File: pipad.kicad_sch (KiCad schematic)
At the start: 2 parts, among them J3 Conn_02x20_Odd_Even, J5 Conn_01x03

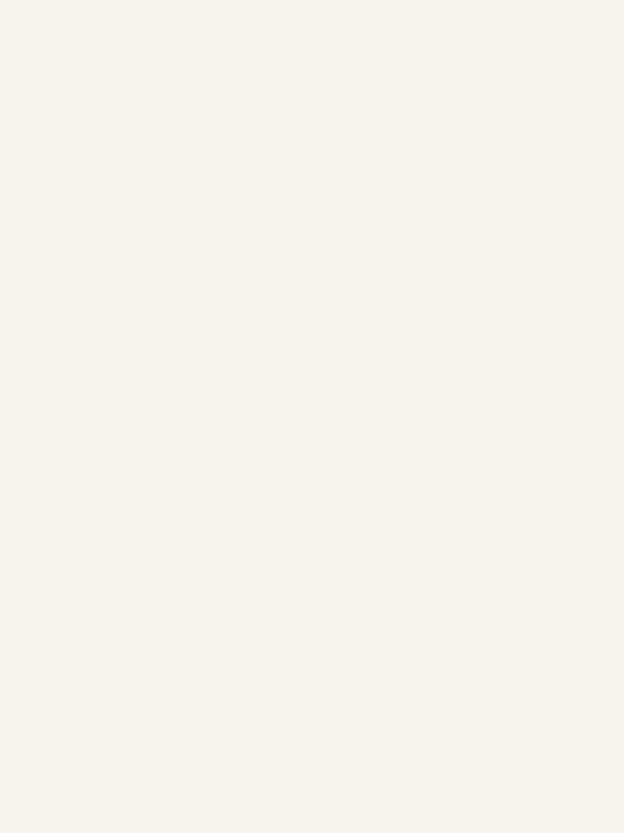
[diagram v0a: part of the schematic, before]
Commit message: refactor gt9113_breakout into hierarchical sheet.
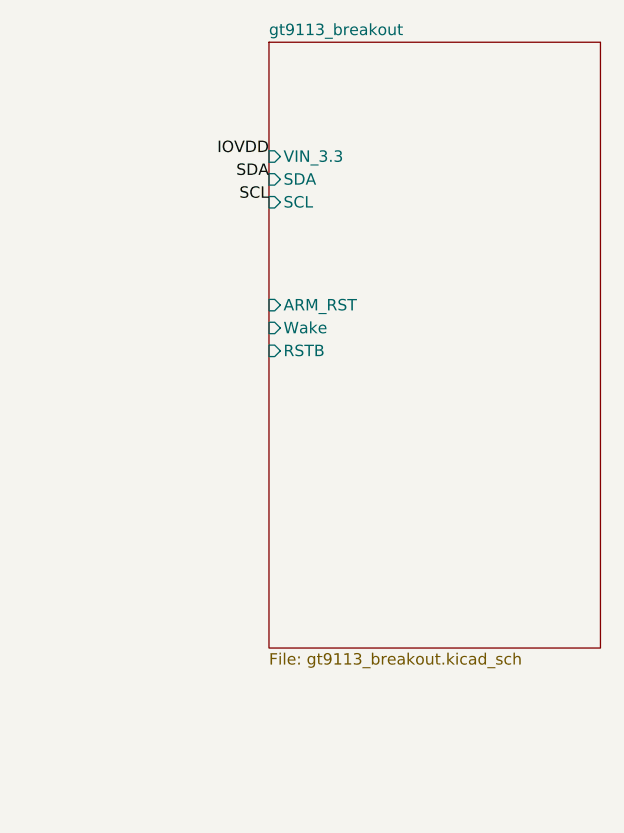
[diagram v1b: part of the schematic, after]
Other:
- added sheet gt9113_breakout (gt9113_breakout.kicad_sch)
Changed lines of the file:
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@@
     (effects (font (size 1.27 1.27)) (justify left bottom))
+  )
+  (label "IOVDD" (at 167.64 50.8 180)
+    (effects (font (size 1.27 1.27)) (justify right bottom))
+  )
+  (label "SDA" (at 167.64 53.34 180)
+    (effects (font (size 1.27 1.27)) (justify right bottom))
+  )
+  (label "SCL" (at 167.64 55.88 180)
+    (effects (font (size 1.27 1.27)) (justify right bottom))
   )
   (symbol (lib_id "power:PWR_FLAG") (at 34.29 156.21 0) (unit 1)
@@
     )
   )
+  (sheet (at 167.64 38.1) (size 36.83 67.31) (fields_autoplaced)
+    (stroke (width 0.0006) (type solid) (color 0 0 0 0))
+    (fill (color 0 0 0 0.0000))
+    (property "Sheet name" "gt9113_breakout" (id 0) (at 167.64 37.4643 0)
+      (effects (font (size 1.27 1.27)) (justify left bottom))
+    )
+    (property "Sheet file" "gt9113_breakout.kicad_sch" (id 1) (at 167.64 105.9187 0)
+      (effects (font (size 1.27 1.27)) (justify left top))
+    )
+    (pin "VIN_3.3" input (at 167.64 50.8 180)
+      (effects (font (size 1.27 1.27)) (justify left))
+    )
+    (pin "SDA" input (at 167.64 53.34 180)
+      (effects (font (size 1.27 1.27)) (justify left))
+    )
+    (pin "SCL" input (at 167.64 55.88 180)
+      (effects (font (size 1.27 1.27)) (justify left))
+    )
+    (pin "ARM_RST" input (at 167.64 67.31 180)
+      (effects (font (size 1.27 1.27)) (justify left))
+    )
+    (pin "Wake" input (at 167.64 69.85 180)
+      (effects (font (size 1.27 1.27)) (justify left))
+    )
+    (pin "RSTB" input (at 167.64 72.39 180)
+      (effects (font (size 1.27 1.27)) (justify left))
+    )
+  )
   (sheet_instances
     (path "/" (page "1"))
     (path "/00000000-0000-0000-0000-00006026a3be/" (page "2"))
     (path "/00000000-0000-0000-0000-00006026a3be/00000000-0000-0000-0000-000060276bea/" (page "4"))
+    (path "/4ecc04d7-c0c4-4778-83ba-d295a895ebe9/" (page "5"))
     (path "/00000000-0000-0000-0000-00006026a3be/e9fc4bb6-5bde-4905-9630-250663643427/" (page " "))
   )
@@
       (reference "U3") (unit 1) (value "TPA2006D1DRBR") (footprint "footprints:TPA2006D1DRBR")
     )
+    (path "/4ecc04d7-c0c4-4778-83ba-d295a895ebe9/00000000-0000-0000-0000-0000600d74cd"
+      (reference "#FLG0102") (unit 1) (value "PWR_FLAG") (footprint "")
+    )
+    (path "/4ecc04d7-c0c4-4778-83ba-d295a895ebe9/00000000-0000-0000-0000-000060028f86"
+      (reference "#PWR010") (unit 1) (value "GND") (footprint "")
+    )
+    (path "/4ecc04d7-c0c4-4778-83ba-d295a895ebe9/00000000-0000-0000-0000-000060029001"
+      (reference "#PWR023") (unit 1) (value "GND") (footprint "")
+    )
+    (path "/4ecc04d7-c0c4-4778-83ba-d295a895ebe9/00000000-0000-0000-0000-000060029007"
+      (reference "#PWR033") (unit 1) (value "GND") (footprint "")
+    )
+    (path "/4ecc04d7-c0c4-4778-83ba-d295a895ebe9/00000000-0000-0000-0000-0000603613b4"
+      (reference "#PWR0101") (unit 1) (value "GND") (footprint "")
+    )
+    (path "/4ecc04d7-c0c4-4778-83ba-d295a895ebe9/00000000-0000-0000-0000-0000603614b1"
+      (reference "#PWR0102") (unit 1) (value "GND") (footprint "")
+    )
+    (path "/4ecc04d7-c0c4-4778-83ba-d295a895ebe9/00000000-0000-0000-0000-0000604218d4"
+      (reference "#PWR0103") (unit 1) (value "GND") (footprint "")
+    )
+    (path "/4ecc04d7-c0c4-4778-83ba-d295a895ebe9/00000000-0000-0000-0000-00006042145b"
+      (reference "#PWR0104") (unit 1) (value "GND") (footprint "")
+    )
+    (path "/4ecc04d7-c0c4-4778-83ba-d295a895ebe9/00000000-0000-0000-0000-0000604214a2"
+      (reference "#PWR0105") (unit 1) (value "GND") (footprint "")
+    )
+    (path "/4ecc04d7-c0c4-4778-83ba-d295a895ebe9/00000000-0000-0000-0000-00006042f1b0"
+      (reference "#PWR0106") (unit 1) (value "GND") (footprint "")
+    )
+    (path "/4ecc04d7-c0c4-4778-83ba-d295a895ebe9/00000000-0000-0000-0000-0000604338e7"
+      (reference "#PWR0107") (unit 1) (value "GND") (footprint "")
+    )
+    (path "/4ecc04d7-c0c4-4778-83ba-d295a895ebe9/00000000-0000-0000-0000-000060439719"
+      (reference "#PWR0108") (unit 1) (value "GND") (footprint "")
+    )
+    (path "/4ecc04d7-c0c4-4778-83ba-d295a895ebe9/00000000-0000-0000-0000-00006041d916"
+      (reference "C1") (unit 1) (value "2.2uF") (footprint "Capacitor_SMD:C_0402_1005Metric")
+    )
+    (path "/4ecc04d7-c0c4-4778-83ba-d295a895ebe9/00000000-0000-0000-0000-00006041dee8"
+      (reference "C2") (unit 1) (value "2.2uF") (footprint "Capacitor_SMD:C_0402_1005Metric")
+    )
+    (path "/4ecc04d7-c0c4-4778-83ba-d295a895ebe9/00000000-0000-0000-0000-00006041e2b4"
+      (reference "C3") (unit 1) (value "2.2uF") (footprint "Capacitor_SMD:C_0402_1005Metric")
+    )
+    (path "/4ecc04d7-c0c4-4778-83ba-d295a895ebe9/00000000-0000-0000-0000-000060049eec"
+      (reference "J1") (unit 1) (value "Conn_01x09_Male") (footprint "Connector_PinHeader_2.54mm:PinHeader_1x09_P2.54mm_Vertical")
+    )
+    (path "/4ecc04d7-c0c4-4778-83ba-d295a895ebe9/00000000-0000-0000-0000-000060028f6e"
+      (reference "J7") (unit 1) (value "504740-5100") (footprint "footprints:504740-5100")
+    )
+    (path "/4ecc04d7-c0c4-4778-83ba-d295a895ebe9/00000000-0000-0000-0000-000060028f74"
+      (reference "J7") (unit 1) (value "504740-5100") (footprint "footprints:504740-5100")
+    )
+    (path "/4ecc04d7-c0c4-4778-83ba-d295a895ebe9/00000000-0000-0000-0000-000060028f7a"
+      (reference "J8") (unit 1) (value "504740-5100") (footprint "footprints:504740-5100")
+    )
+    (path "/4ecc04d7-c0c4-4778-83ba-d295a895ebe9/00000000-0000-0000-0000-000060028f80"
+      (reference "J8") (unit 1) (value "504740-5100") (footprint "footprints:504740-5100")
+    )
+    (path "/4ecc04d7-c0c4-4778-83ba-d295a895ebe9/00000000-0000-0000-0000-000060432c0a"
+      (reference "R1") (unit 1) (value "0R/DNF") (footprint "Resistor_SMD:R_0402_1005Metric")
+    )
+    (path "/4ecc04d7-c0c4-4778-83ba-d295a895ebe9/00000000-0000-0000-0000-0000604322a7"
+      (reference "R2") (unit 1) (value "0R/DNF") (footprint "Resistor_SMD:R_0402_1005Metric")
+    )
+    (path "/4ecc04d7-c0c4-4778-83ba-d295a895ebe9/00000000-0000-0000-0000-000060427deb"
+      (reference "R3") (unit 1) (value "300k/DNF") (footprint "Resistor_SMD:R_0402_1005Metric")
+    )
+    (path "/4ecc04d7-c0c4-4778-83ba-d295a895ebe9/00000000-0000-0000-0000-000060371774"
+      (reference "U1") (unit 1) (value "GT9113") (footprint "footprints:GT9113")
+    )
     (path "/00000000-0000-0000-0000-00006026a3be/e9fc4bb6-5bde-4905-9630-250663643427/fd649b90-fe8e-4ecf-a531-c62c874ce18c"

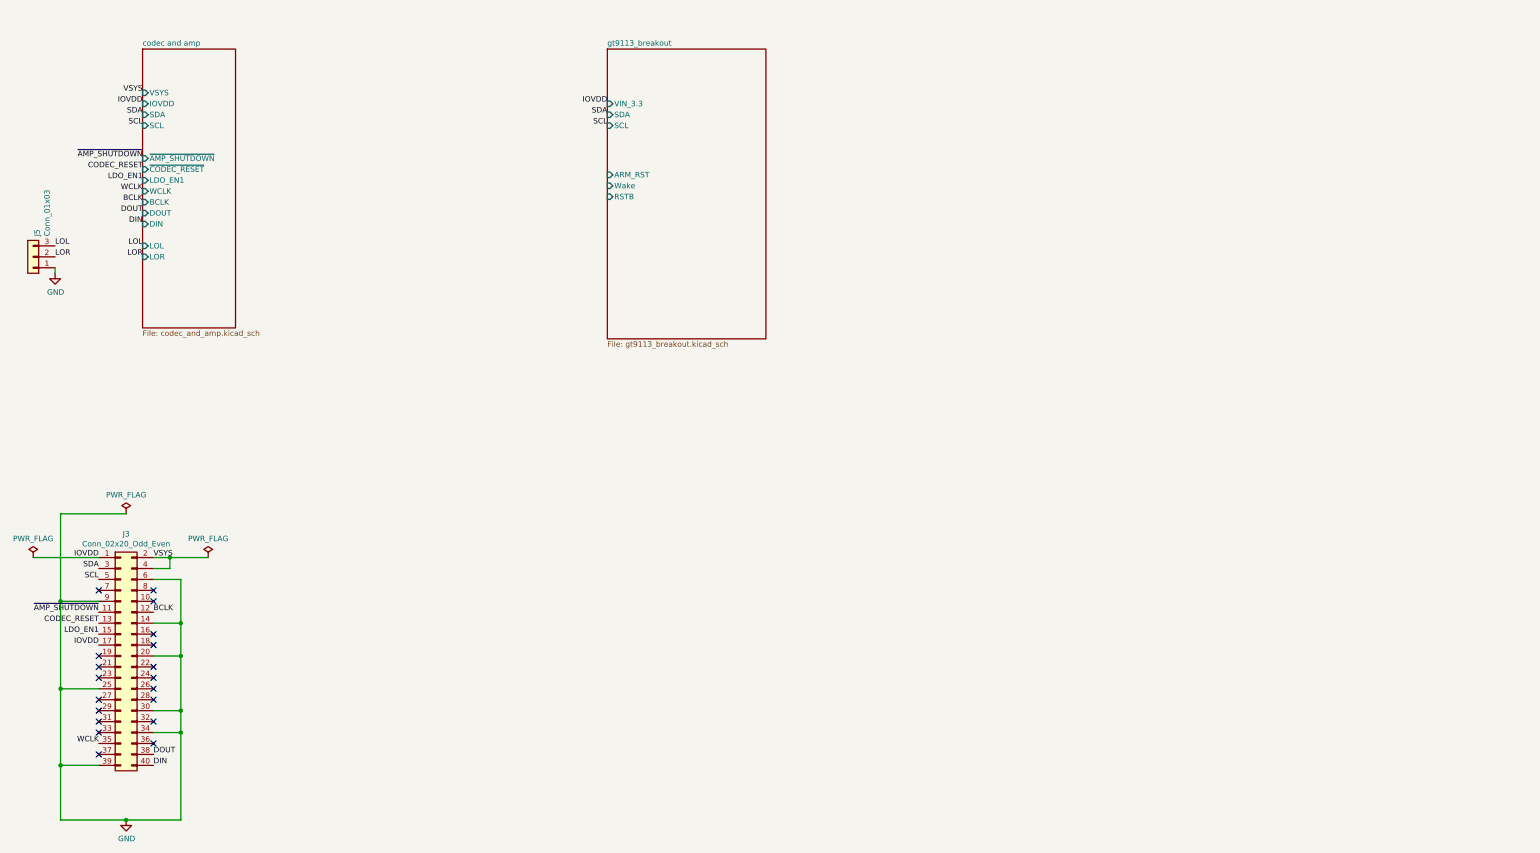
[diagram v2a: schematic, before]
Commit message: Import LVDS schematic as hierarchical sheet. Add level shifters for I2C and EN/IRQ pins.
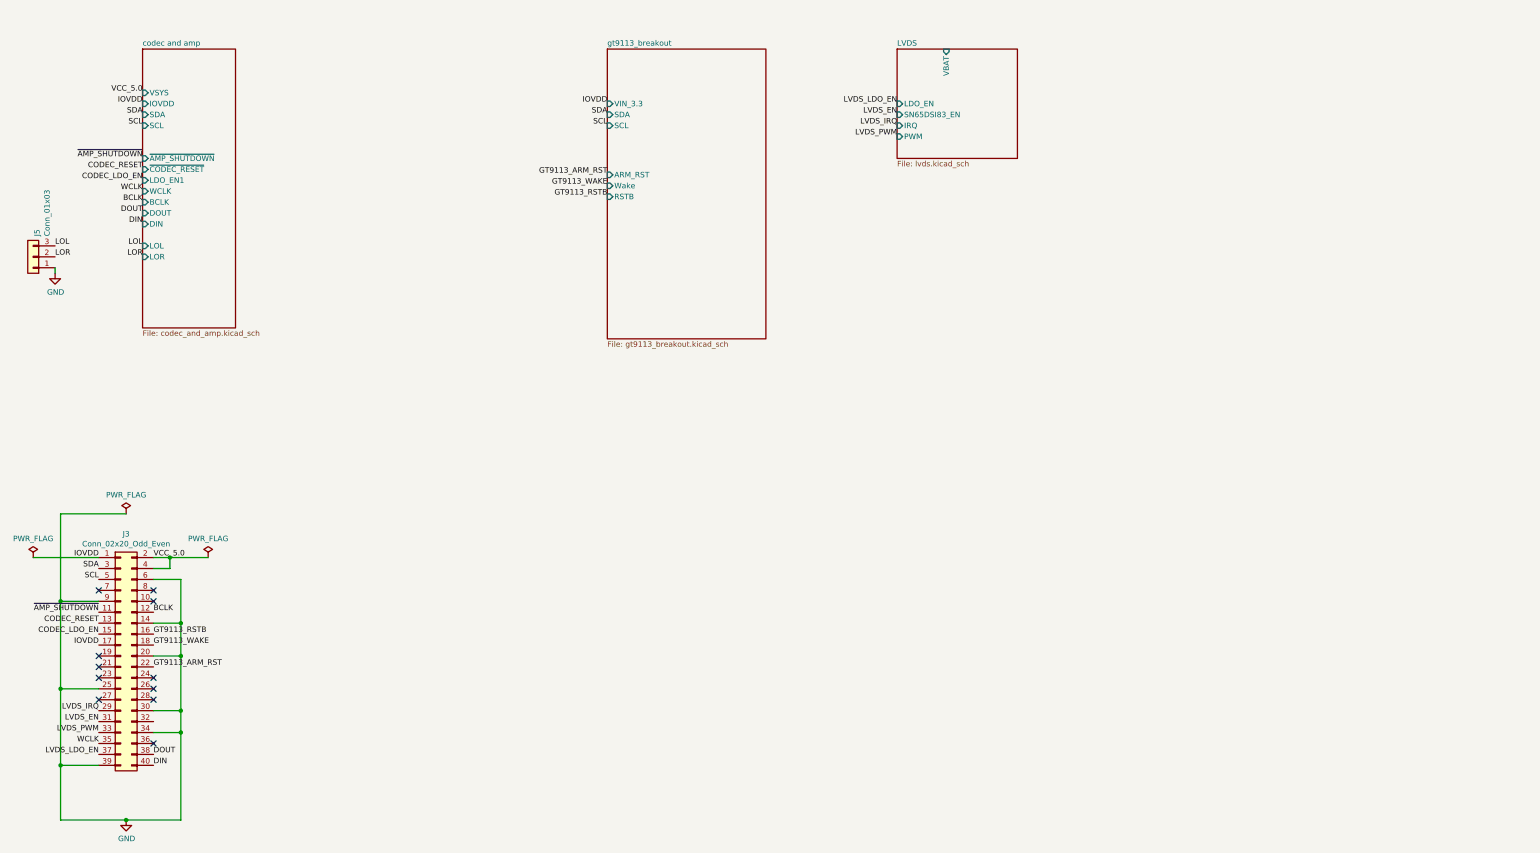
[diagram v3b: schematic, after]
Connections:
- net GT9113_RSTB: now reaches J3.16 (Pin_16)
- net GT9113_WAKE: now reaches J3.18 (Pin_18)
- net GT9113_ARM_RST: now reaches J3.22 (Pin_22)
- net LVDS_IRQ: now reaches J3.29 (Pin_29)
- net LVDS_EN: now reaches J3.31 (Pin_31)
- net LVDS_PWM: now reaches J3.33 (Pin_33)
- net LVDS_LDO_EN: now reaches J3.37 (Pin_37)
- net LDO_EN1 renamed CODEC_LDO_EN
- net VSYS renamed VCC_5.0
- no-connect marks 19 -> 11
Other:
- added sheet LVDS (lvds.kicad_sch)
